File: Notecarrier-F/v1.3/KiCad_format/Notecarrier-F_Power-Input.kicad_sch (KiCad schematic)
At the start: 21 parts, among them J1 S2BPHSM4TBLFSN, J2 S2BPHSM4TBLFSN, J3 S2BPHSM4TBLFSN, J4 10118193-0001LF, U2 BQ24210DQCT

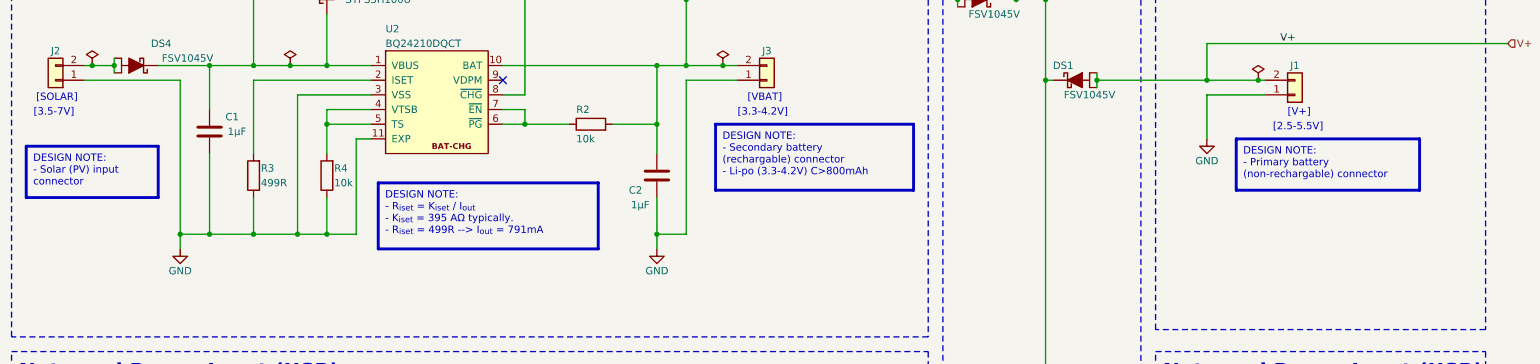
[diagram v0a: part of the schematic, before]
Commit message: Notecarrier-F: convert its design-note text_boxes too
The first conversion pass scoped by red-frame rectangles and missed
Notecarrier-F: its 16 notes have no separate frame - the text_box itself draws
a 0.5mm red border - so they were entirely invisible on the published pages,
frames included. Same conversion as 25a2d84, with two additions the F notes
forced:

- KiCad's hidden PDF text layer mangles special glyphs (broken ToUnicode maps
  for u/~/ohm produce mojibake) and F's notes are full of them, so exact
  word-matching is unattainable. Notes whose visual line count matches their
  source line count need no wrap-freezing at all and are kept verbatim, guarded
  by a per-line ASCII similarity check; only genuinely wrapped notes use the
  strict word-level path, and F's wrapped notes are clean of special glyphs.
  The converter also now rebuilds output from SOURCE words - the PDF only
  supplies break positions - so KiCad markup like R_{iset} stays markup in the
  file instead of being replaced by its rendered form.

- The F author gave these notes an explicit black font color. Black is what
  KiCad plots either way, but explicit black is invisible on a dark-theme
  viewer. The 16 notes now carry no explicit color, like every other board's
  notes: KiCad plots its default dark blue, kicanvas its theme color. This is
  the one deliberate visual change - note text black -> dark blue in KiCad -
  and it makes F consistent with the other five boards.

Netlist byte-equal before and after; kicanvas renders all four modified sheets
with the notes visible and the subscript markup intact.

Co-Authored-By: Claude Fable 5 <noreply@anthropic.com>
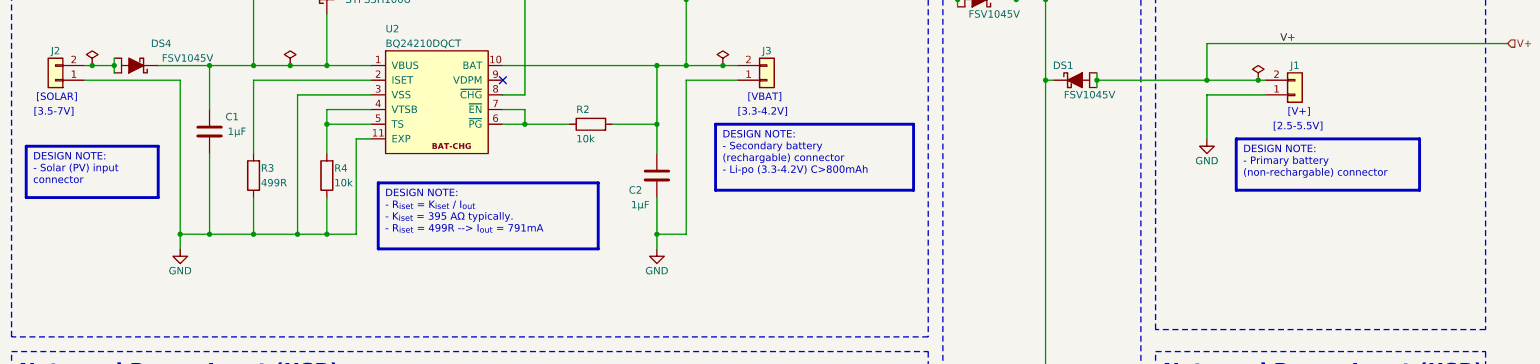
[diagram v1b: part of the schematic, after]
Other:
- note added: "DESIGN NOTE: - Primary battery (non-rechargable) connector"
- note added: "DESIGN NOTE: - R_{iset} = K_{iset} / I_{out} - K_{iset} = 395 AΩ typically. - R_{iset} = 499R --> I_{out} = 791mA"
- note added: "DESIGN NOTE: - Secondary battery (rechargable) connector - Li-po (3.3-4.2V) C>800mAh"
- note added: "DESIGN NOTE: - Solar (PV) input connector"
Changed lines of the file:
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@@
 		)
 	)
-	(text_box "DESIGN NOTE:\n- Primary battery (non-rechargable) connector"
-		(exclude_from_sim no)
-		(at 227.33 68.58 0)
-		(size 31.75 8.89)
-		(margins 1.2025 1.2025 1.2025 1.2025)
+	(rectangle
+		(start 227.33 68.58)
+		(end 259.08 77.47)
 		(stroke
 			(width 0.5)
@@
 			(type none)
 		)
+	)
+	(text "DESIGN NOTE:\n- Primary battery\n(non-rechargable) connector"
+		(exclude_from_sim no)
+		(at 228.532 69.7825 0)
 		(effects
 			(font
 				(size 1.27 1.27)
-				(color 0 0 0 1)
 			)
 			(justify left top)
 		)
 	)
-	(text_box "DESIGN NOTE:\n- Secondary battery (rechargable) connector\n- Li-po (3.3-4.2V) C>800mAh"
-		(exclude_from_sim no)
-		(at 137.16 66.04 0)
-		(size 34.29 11.43)
-		(margins 1.2025 1.2025 1.2025 1.2025)
+	(rectangle
+		(start 137.16 66.04)
+		(end 171.45 77.47)
 		(stroke
 			(width 0.5)
@@
 			(type none)
 		)
+	)
+	(text "DESIGN NOTE:\n- Secondary battery\n(rechargable) connector\n- Li-po (3.3-4.2V) C>800mAh"
+		(exclude_from_sim no)
+		(at 138.362 67.2425 0)
 		(effects
 			(font
 				(size 1.27 1.27)
-				(color 0 0 0 1)
 			)
 			(justify left top)
 		)
 	)
-	(text_box "DESIGN NOTE:\n- R_{iset} = K_{iset} / I_{out}\n- K_{iset} = 395 AΩ typically.\n- R_{iset} = 499R --> I_{out} = 791mA"
-		(exclude_from_sim no)
-		(at 78.74 76.2 0)
-		(size 38.1 11.43)
-		(margins 1.2025 1.2025 1.2025 1.2025)
+	(rectangle
+		(start 78.74 76.2)
+		(end 116.84 87.63)
 		(stroke
 			(width 0.5)
@@
 			(type none)
 		)
+	)
+	(text "DESIGN NOTE:\n- R_{iset} = K_{iset} / I_{out}\n- K_{iset} = 395 AΩ typically.\n- R_{iset} = 499R --> I_{out} = 791mA"
+		(exclude_from_sim no)
+		(at 79.9425 77.4025 0)
 		(effects
 			(font
 				(size 1.27 1.27)
-				(color 0 0 0 1)
 			)
 			(justify left top)
 		)
 	)
-	(text_box "DESIGN NOTE:\n- Solar (PV) input connector"
-		(exclude_from_sim no)
-		(at 17.78 69.85 0)
-		(size 22.86 8.89)
-		(margins 1.2025 1.2025 1.2025 1.2025)
+	(rectangle
+		(start 17.78 69.85)
+		(end 40.64 78.74)
 		(stroke
 			(width 0.5)
@@
 			(type none)
 		)
+	)
+	(text "DESIGN NOTE:\n- Solar (PV) input\nconnector"
+		(exclude_from_sim no)
+		(at 18.9825 71.0525 0)
 		(effects
 			(font
 				(size 1.27 1.27)
-				(color 0 0 0 1)
 			)
 			(justify left top)
